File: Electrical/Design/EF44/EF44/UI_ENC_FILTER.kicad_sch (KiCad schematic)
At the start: 10 parts

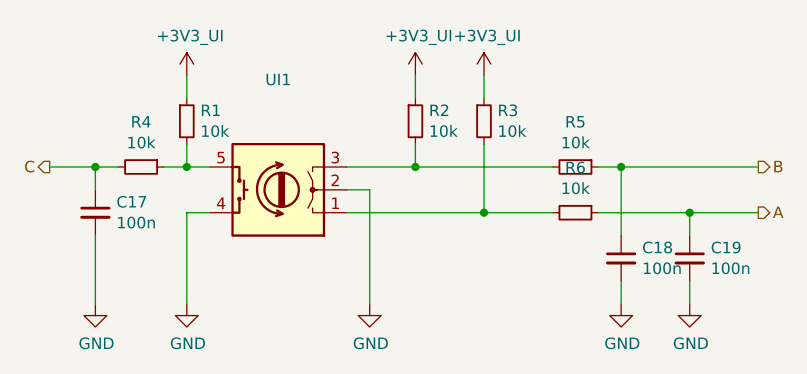
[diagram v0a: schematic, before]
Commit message: SUKU EF44 created from EN16 Base
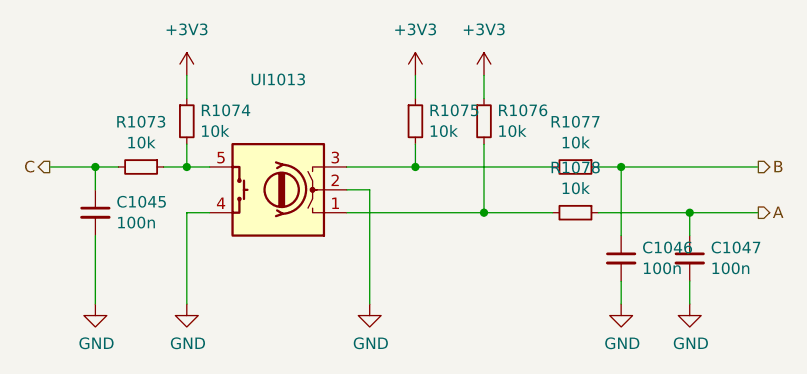
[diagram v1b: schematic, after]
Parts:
- C1045: renamed from C17; footprint suku_basics:CAP_0805 -> suku_basics:CAP_0402
- C1046: renamed from C18; footprint suku_basics:CAP_0805 -> suku_basics:CAP_0402
- C1047: renamed from C19; footprint suku_basics:CAP_0805 -> suku_basics:CAP_0402
- R1073: renamed from R4; footprint suku_basics:RES_0805 -> suku_basics:RES_0402
- R1074: renamed from R1; footprint suku_basics:RES_0805 -> suku_basics:RES_0402
- R1075: renamed from R2; footprint suku_basics:RES_0805 -> suku_basics:RES_0402
- R1076: renamed from R3; footprint suku_basics:RES_0805 -> suku_basics:RES_0402
- R1077: renamed from R5; footprint suku_basics:RES_0805 -> suku_basics:RES_0402
- R1078: renamed from R6; footprint suku_basics:RES_0805 -> suku_basics:RES_0402
- renumbered UI1 to UI1013
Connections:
- net +3V3_UI renamed +3V3

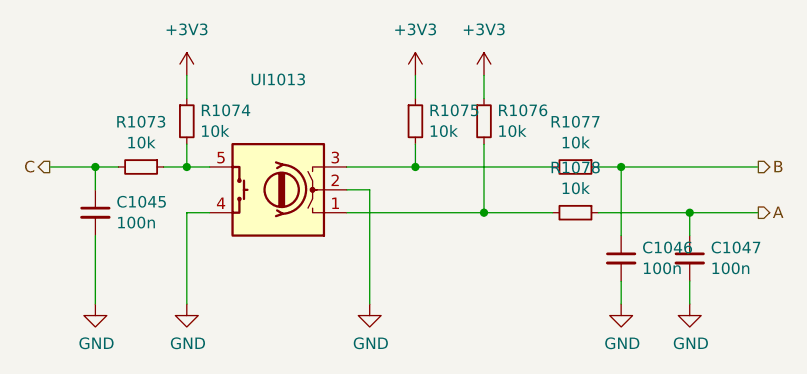
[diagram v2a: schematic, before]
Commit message: SUKU EF44 routing done
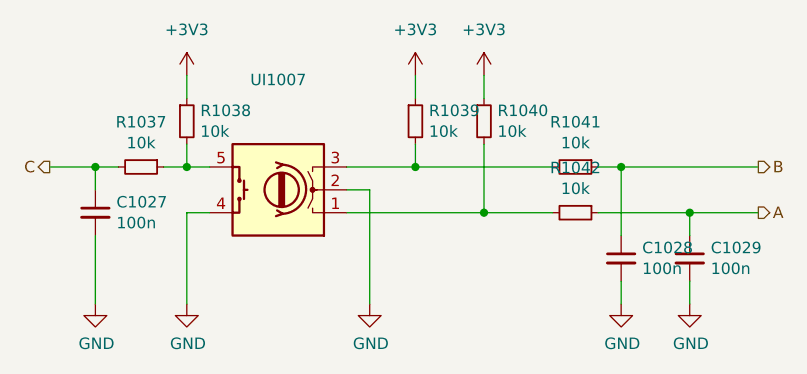
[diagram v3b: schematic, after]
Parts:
- renumbered C1045 to C1027, C1046 to C1028, C1047 to C1029, R1073 to R1037, R1074 to R1038, R1075 to R1039, R1076 to R1040, R1077 to R1041, R1078 to R1042, UI1013 to UI1007
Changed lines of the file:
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@@
   (symbol (lib_id "power:GND") (at 83.82 68.58 0) (unit 1)
     (in_bom yes) (on_board yes) (dnp no)
-    (property "Reference" "#PWR01140" (at 83.82 74.93 0)
+    (property "Reference" "#PWR01092" (at 83.82 74.93 0)
       (effects (font (size 1.27 1.27)) hide)
     )
@@
   (symbol (lib_id "suku_basics:RES") (at 106.68 53.34 270) (unit 1)
     (in_bom yes) (on_board yes) (dnp no)
-    (property "Reference" "R1077" (at 106.68 48.3616 90)
+    (property "Reference" "R1041" (at 106.68 48.3616 90)
       (effects (font (size 1.27 1.27)))
     )
@@
   (symbol (lib_id "suku_basics:RES") (at 88.9 48.26 0) (unit 1)
     (in_bom yes) (on_board yes) (dnp no)
-    (property "Reference" "R1075" (at 90.3986 47.0916 0)
+    (property "Reference" "R1039" (at 90.3986 47.0916 0)
       (effects (font (size 1.27 1.27)) (justify left))
     )
@@
   (symbol (lib_id "suku_basics:UI_Rotary_Encoder_Switch") (at 73.66 55.88 180) (unit 1)
     (in_bom yes) (on_board yes) (dnp no)
-    (property "Reference" "UI1013" (at 73.66 43.6626 0)
+    (property "Reference" "UI1007" (at 73.66 43.6626 0)
       (effects (font (size 1.27 1.27)))
     )
@@
   (symbol (lib_id "suku_basics:CAP") (at 111.76 63.5 0) (unit 1)
     (in_bom yes) (on_board yes) (dnp no)
-    (property "Reference" "C1046" (at 114.0968 62.3316 0)
+    (property "Reference" "C1028" (at 114.0968 62.3316 0)
       (effects (font (size 1.27 1.27)) (justify left))
     )
@@
   (symbol (lib_id "power:GND") (at 111.76 68.58 0) (unit 1)
     (in_bom yes) (on_board yes) (dnp no)
-    (property "Reference" "#PWR01143" (at 111.76 74.93 0)
+    (property "Reference" "#PWR01095" (at 111.76 74.93 0)
       (effects (font (size 1.27 1.27)) hide)
     )
@@
   (symbol (lib_id "suku_basics:RES") (at 96.52 48.26 0) (unit 1)
     (in_bom yes) (on_board yes) (dnp no)
-    (property "Reference" "R1076" (at 98.0186 47.0916 0)
+    (property "Reference" "R1040" (at 98.0186 47.0916 0)
       (effects (font (size 1.27 1.27)) (justify left))
     )
@@
   (symbol (lib_id "suku_basics:CAP") (at 119.38 63.5 0) (unit 1)
     (in_bom yes) (on_board yes) (dnp no)
-    (property "Reference" "C1047" (at 121.7168 62.3316 0)
+    (property "Reference" "C1029" (at 121.7168 62.3316 0)
       (effects (font (size 1.27 1.27)) (justify left))
     )
@@
   (symbol (lib_id "power:GND") (at 119.38 68.58 0) (unit 1)
     (in_bom yes) (on_board yes) (dnp no)
-    (property "Reference" "#PWR01144" (at 119.38 74.93 0)
+    (property "Reference" "#PWR01096" (at 119.38 74.93 0)
       (effects (font (size 1.27 1.27)) hide)
     )
@@
   (symbol (lib_id "suku_basics:RES") (at 106.68 58.42 270) (unit 1)
     (in_bom yes) (on_board yes) (dnp no)
-    (property "Reference" "R1078" (at 106.68 53.4416 90)
+    (property "Reference" "R1042" (at 106.68 53.4416 90)
       (effects (font (size 1.27 1.27)))
     )
@@
   (symbol (lib_id "power:GND") (at 63.5 68.58 0) (unit 1)
     (in_bom yes) (on_board yes) (dnp no)
-    (property "Reference" "#PWR01139" (at 63.5 74.93 0)
+    (property "Reference" "#PWR01091" (at 63.5 74.93 0)
       (effects (font (size 1.27 1.27)) hide)
     )
@@
   (symbol (lib_id "suku_basics:RES") (at 63.5 48.26 0) (unit 1)
     (in_bom yes) (on_board yes) (dnp no)
-    (property "Reference" "R1074" (at 64.9986 47.0916 0)
+    (property "Reference" "R1038" (at 64.9986 47.0916 0)
       (effects (font (size 1.27 1.27)) (justify left))
     )
@@
   (symbol (lib_id "suku_basics:RES") (at 58.42 53.34 270) (unit 1)
     (in_bom yes) (on_board yes) (dnp no)
-    (property "Reference" "R1073" (at 58.42 48.3616 90)
+    (property "Reference" "R1037" (at 58.42 48.3616 90)
       (effects (font (size 1.27 1.27)))
     )
@@
   (symbol (lib_id "suku_basics:CAP") (at 53.34 58.42 0) (unit 1)
     (in_bom yes) (on_board yes) (dnp no)
-    (property "Reference" "C1045" (at 55.6768 57.2516 0)
+    (property "Reference" "C1027" (at 55.6768 57.2516 0)
       (effects (font (size 1.27 1.27)) (justify left))
     )
@@
   (symbol (lib_id "power:GND") (at 53.34 68.58 0) (unit 1)
     (in_bom yes) (on_board yes) (dnp no)
-    (property "Reference" "#PWR01137" (at 53.34 74.93 0)
-      (effects (font (size 1.27 1.27)) hide)
-    )
+    (property "Reference" "#PWR01089" (at 53.34 74.93 0)
+      (effects (font (size 1.27 1.27)) hide)
+    )
